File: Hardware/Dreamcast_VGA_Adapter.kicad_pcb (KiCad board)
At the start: 2 copper layers, 56.6 x 57.7 mm, 41 parts, among them J1 AudioJack3, J2 DB15_Female_HighDensity_Mount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, J3 Conn_02x08_Odd_Even, SW1 SW_DIP_x02, U1 THS7316, U2 74HCT2G34

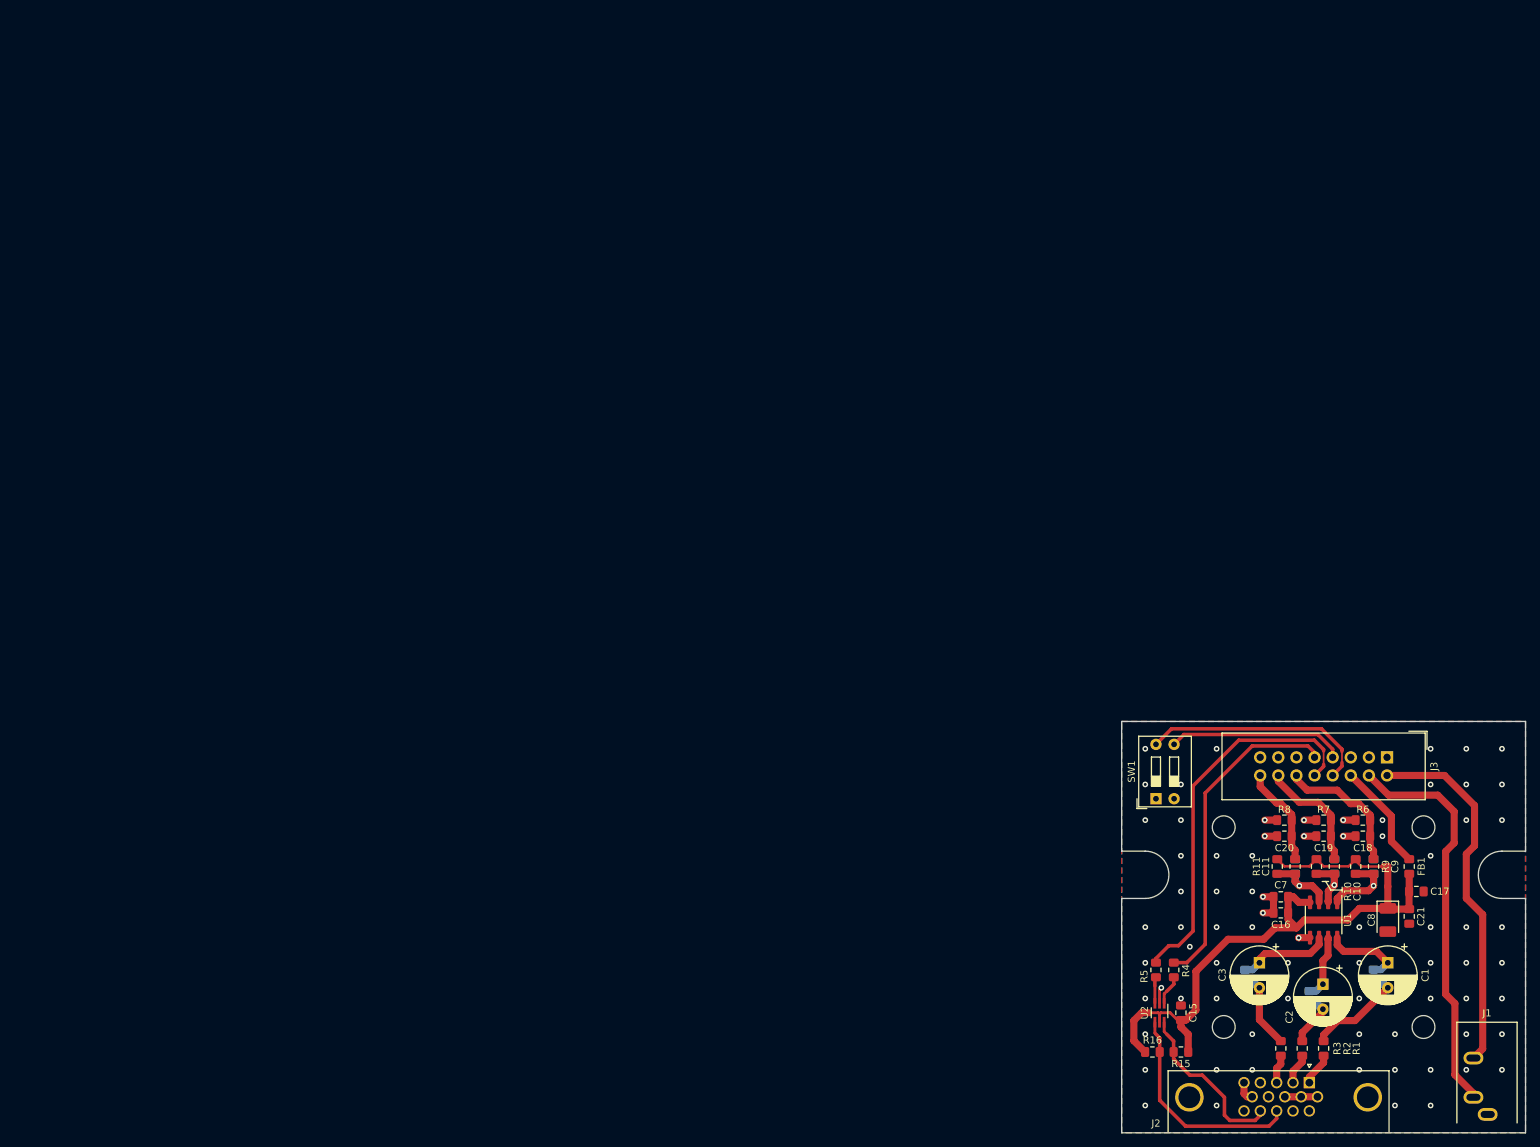
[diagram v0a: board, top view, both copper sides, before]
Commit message: Revert "Created 3D model"
This reverts commit 1b23ede2aa55525ab1088a1304cc43113caee66c.
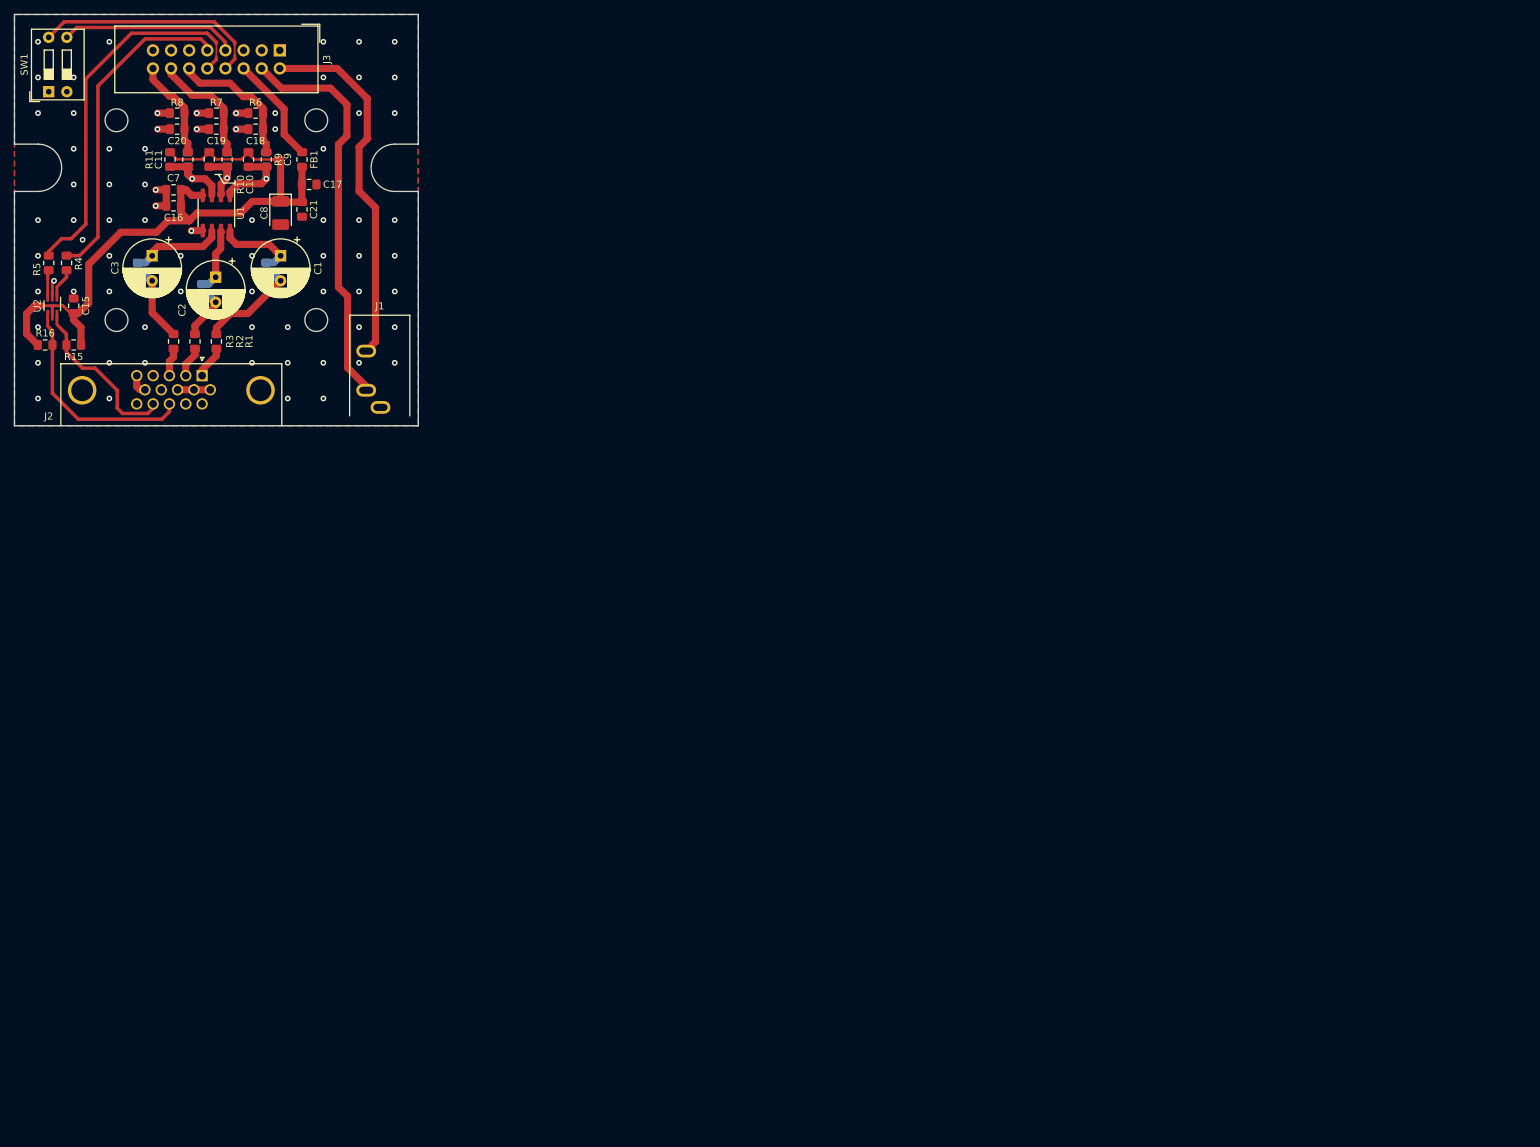
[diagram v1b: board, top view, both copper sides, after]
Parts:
- moved C1 184.1 mm to (9.00, 5.00)
- moved C10 184.1 mm to (1.50, -8.50)
- moved C11 184.1 mm to (-4.00, -8.50)
- moved C15 184.1 mm to (-20.0, 12.0)
- moved C16 184.1 mm to (-6.00, -2.00)
- moved C17 184.1 mm to (13.0, -5.00)
- moved C18 184.1 mm to (5.50, -12.8)
- moved C19 184.1 mm to (0.00, -12.8)
- moved C2 184.1 mm to (-0.10, 8.00)
- moved C20 184.1 mm to (-5.50, -12.8)
- moved C21 184.1 mm to (12.0, -1.50)
- moved C3 184.1 mm to (-9.00, 5.00)
- moved C4 184.1 mm to (7.00, 6.97)
- moved C5 184.1 mm to (-2.00, 10.0)
- moved C6 184.1 mm to (-11.0, 7.00)
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
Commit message: Created 3D model
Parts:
- moved C1 184.1 mm to (164.2, 104.1)
- moved C10 184.1 mm to (156.7, 90.6)
- moved C11 184.1 mm to (151.2, 90.6)
- moved C15 184.1 mm to (135.2, 111.1)
- moved C16 184.1 mm to (149.2, 97.1)
- moved C17 184.1 mm to (168.2, 94.1)
- moved C18 184.1 mm to (160.7, 86.3)
- moved C19 184.1 mm to (155.2, 86.3)
- moved C2 184.1 mm to (155.1, 107.1)
- moved C20 184.1 mm to (149.7, 86.3)
- moved C21 184.1 mm to (167.2, 97.6)
- moved C3 184.1 mm to (146.2, 104.1)
- moved C4 184.1 mm to (162.2, 106.1)
- moved C5 184.1 mm to (153.2, 109.1)
- moved C6 184.1 mm to (144.2, 106.1)
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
